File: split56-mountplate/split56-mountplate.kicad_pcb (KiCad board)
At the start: 2 copper layers, 174.7 x 120.4 mm, 12 parts

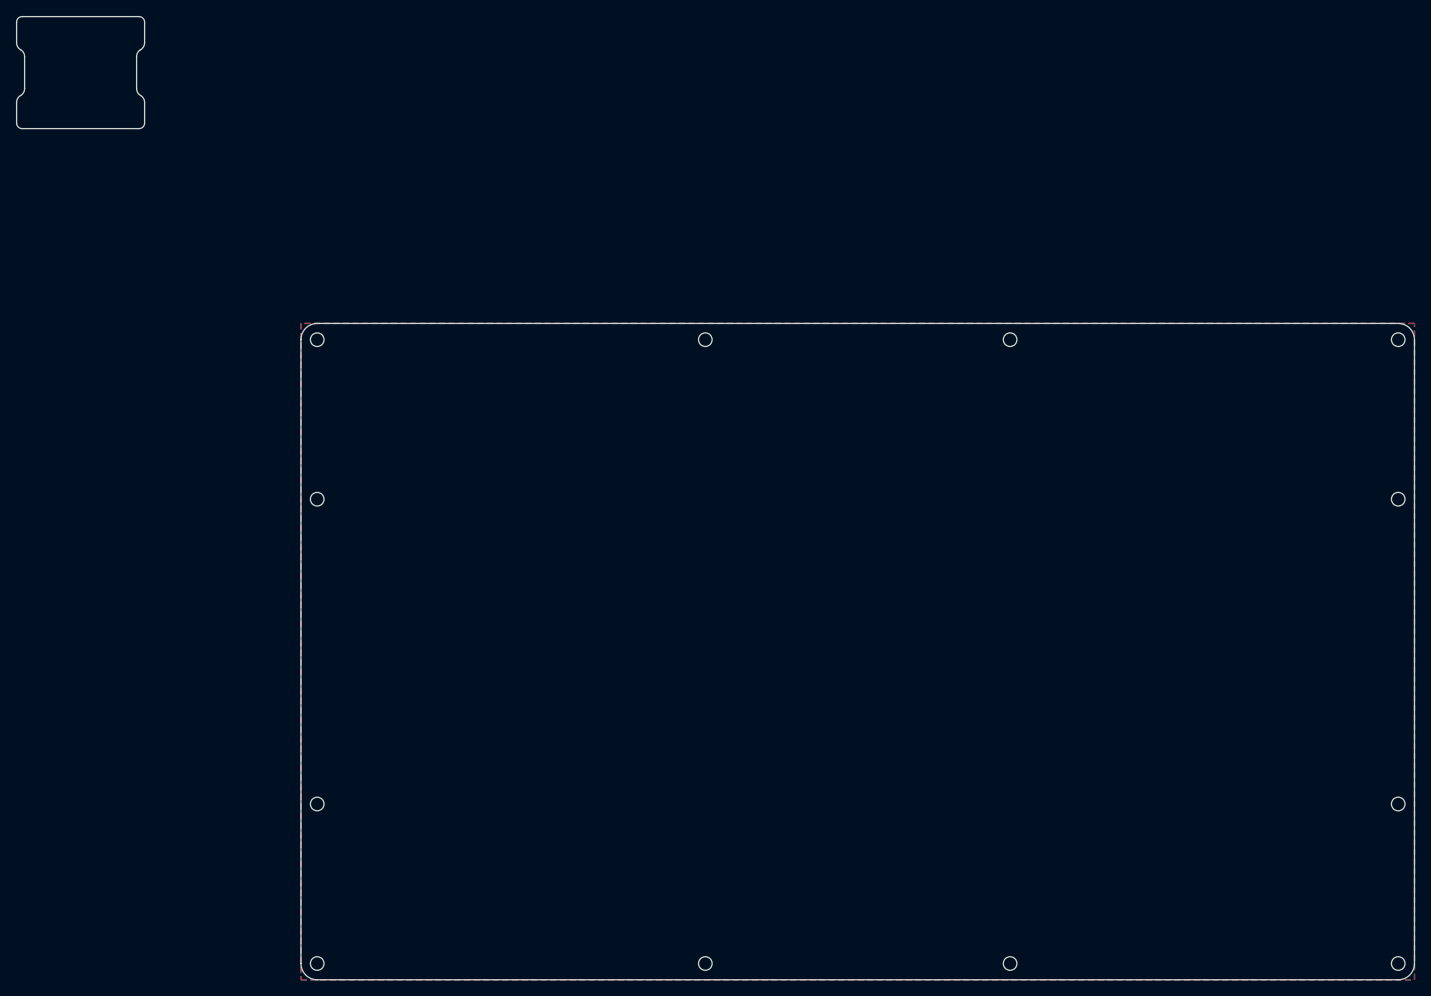
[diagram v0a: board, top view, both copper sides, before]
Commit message: Implement mount plate
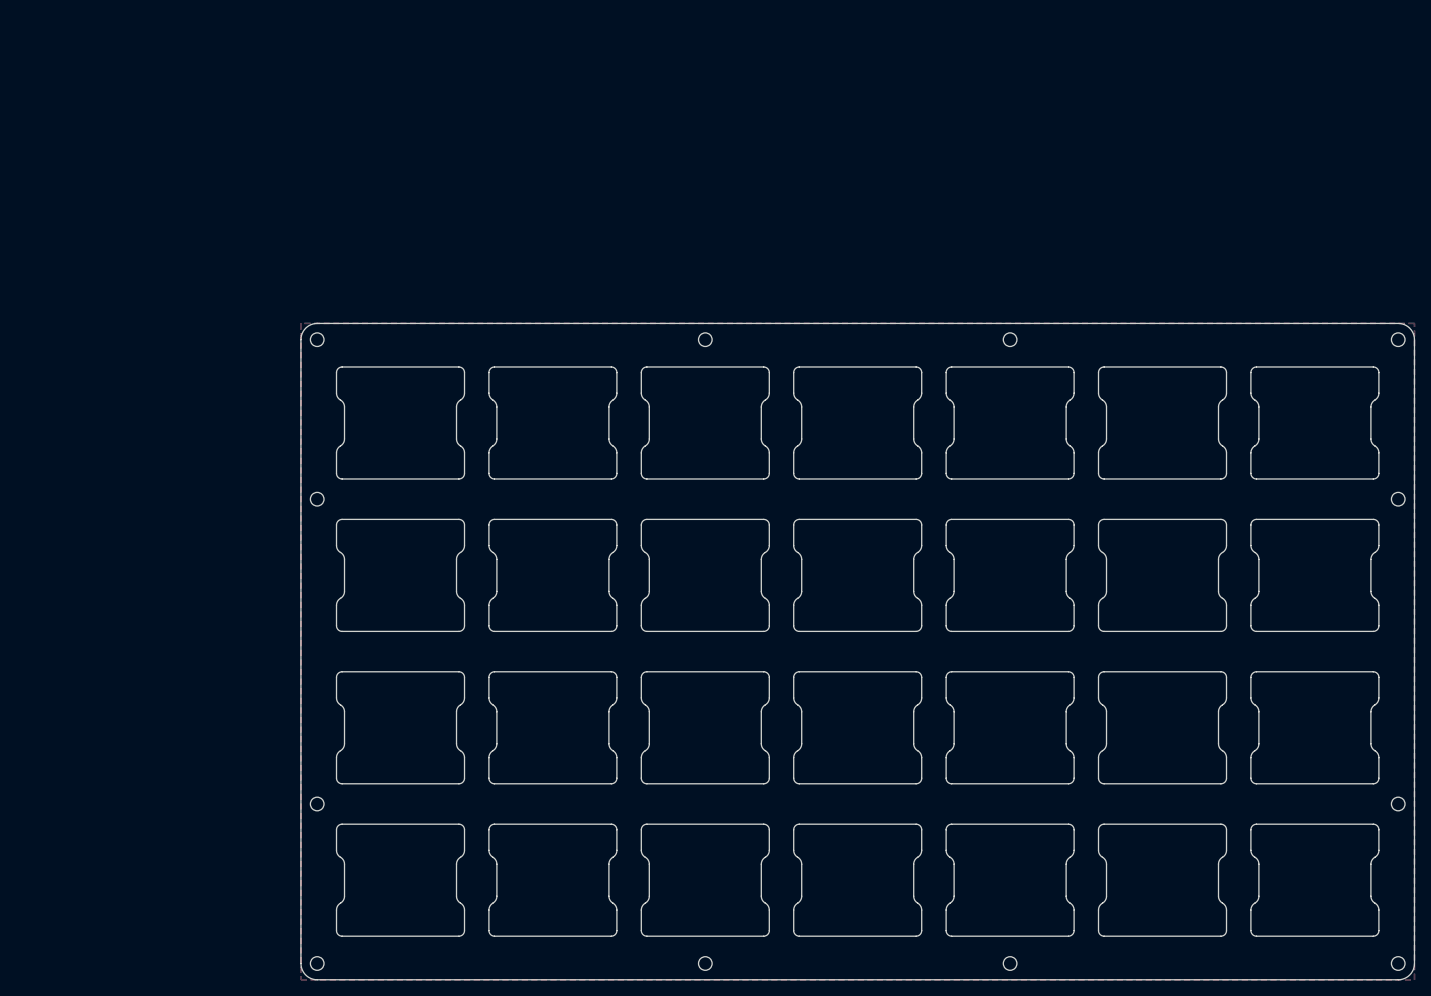
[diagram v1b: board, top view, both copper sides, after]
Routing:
- added copper zone on B.Cu, net (none)
- added copper zone on F.Cu, net (none)
- removed copper zone on B.Cu, net GND
- removed copper zone on F.Cu, net GND
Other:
- board size 174.7 x 120.4 mm -> 139.2 x 82 mm

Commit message: Add GND pour
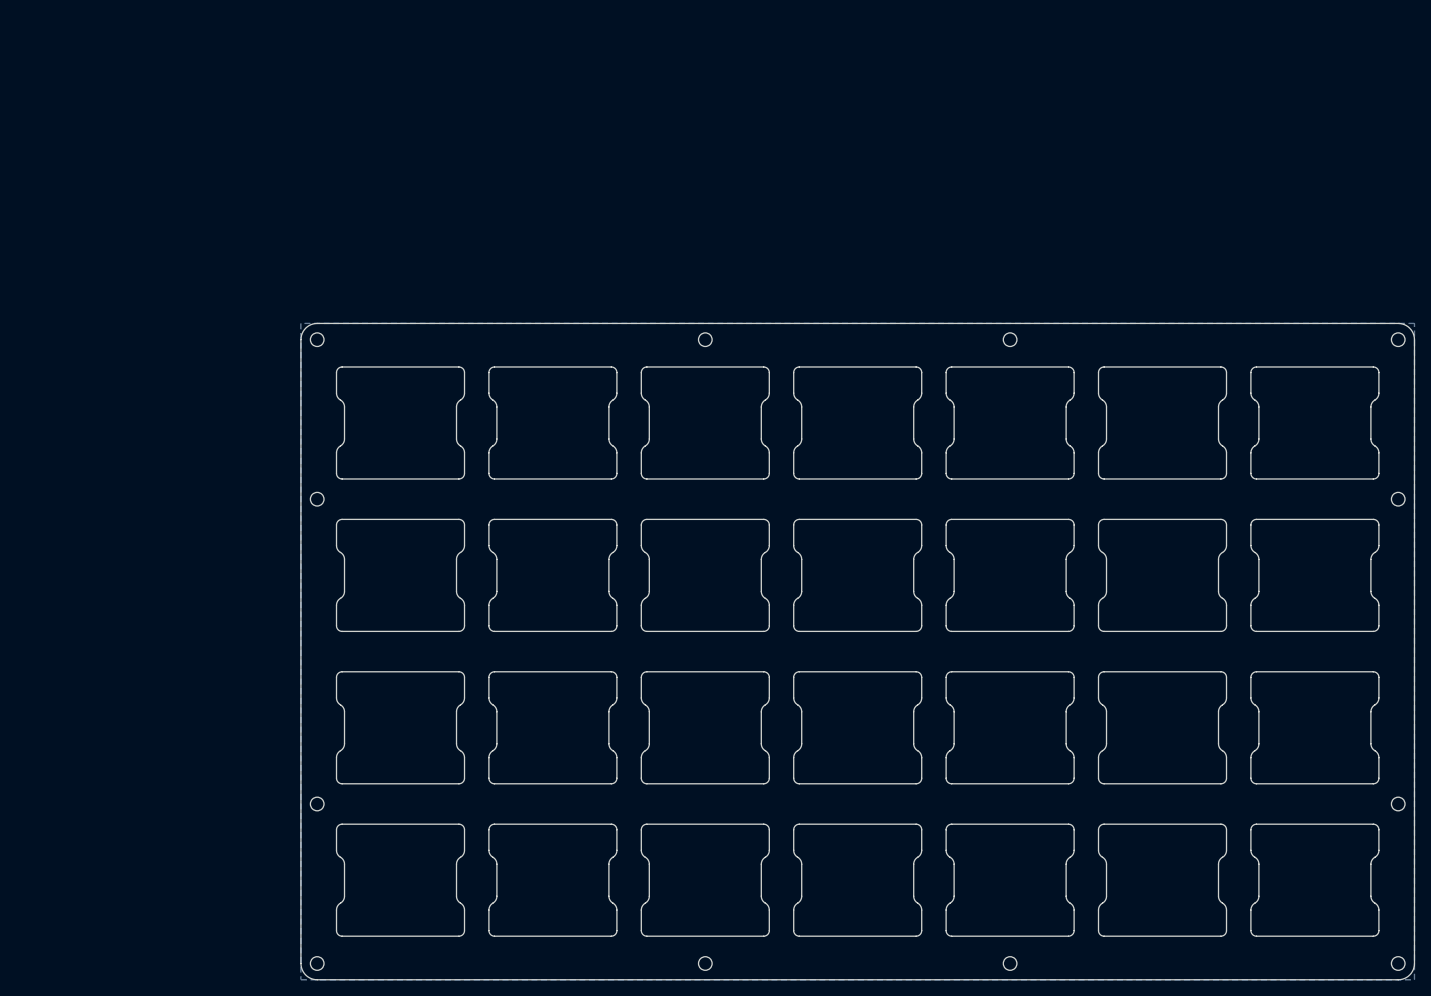
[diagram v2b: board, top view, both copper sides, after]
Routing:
- removed copper zone on F.Cu, net (none)
